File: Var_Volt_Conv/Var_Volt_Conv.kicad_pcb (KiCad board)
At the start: 6 copper layers, 101 x 65 mm, 100 parts, among them J101 Jack-DC, J102 Screw_Terminal_01x02, J103 Screw_Terminal_01x02, J201 Conn_01x05, Q101 AO3416, Q102 IRFML8244TRPBF, Q103 IRFML8244TRPBF, Q104 AO3407, Q105 AO3407, Q106 AO3407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

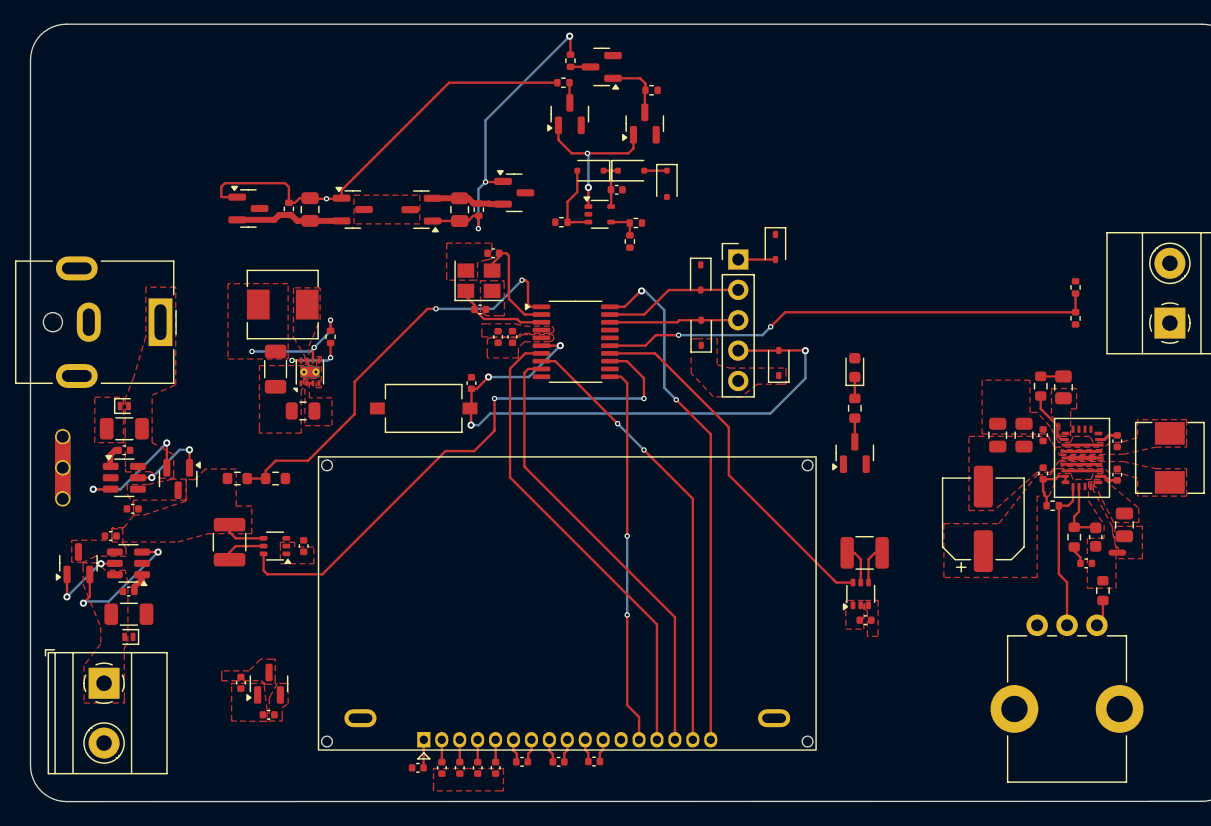
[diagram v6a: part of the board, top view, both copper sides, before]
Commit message: connected all traces, poured all copper pours, passed ERC
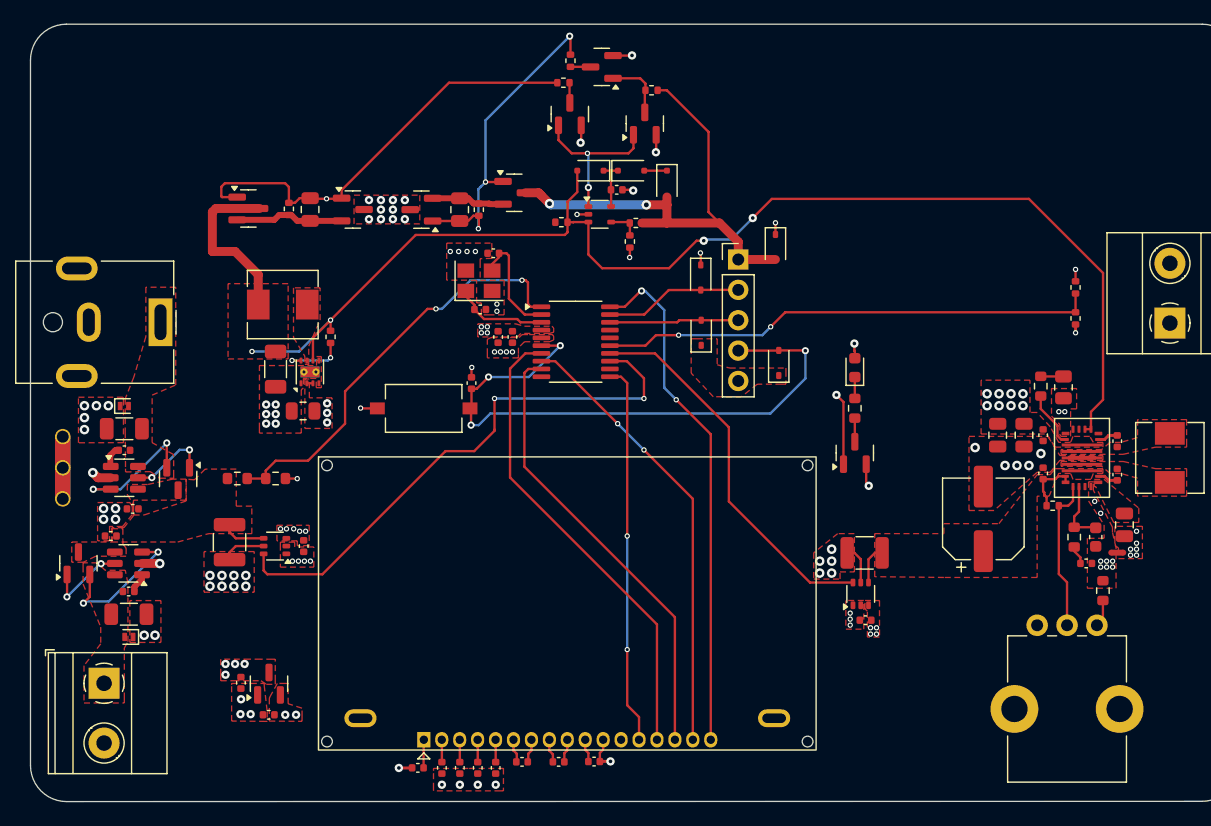
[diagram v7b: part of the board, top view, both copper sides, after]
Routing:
- net /[1] Power/BUCK_VOS: track 16.6 -> 122.4 mm, vias 3 -> 4
- net ST_3V3: track 3.11 -> 41.4 mm, vias 0 -> 2
- net GNDPWR: track 0.00 -> 14.3 mm, vias 0 -> 42
- net +3V3: track 0.00 -> 7.28 mm, vias 0 -> 29
- net GNDD: track 1.94 -> 8.18 mm, vias 0 -> 20
- net S-OUTPUT_CURRENT: track 30.8 -> 31.9 mm
- net VARIABLE_OUTPUT_VOLTAGE_B: track 3.31 -> 4.00 mm, vias 0 -> 6
- net SYSTEM_POWER_B: vias 0 -> 19
- net GNDA: vias 0 -> 17
- net +3V0: vias 0 -> 2
- added copper zone on In2.Cu, net +3V0
- added copper zone on In2.Cu, net +3V3
- added copper zone on In3.Cu, net GNDA
- added copper zone on In4.Cu, net GNDD
- added copper zone on In1.Cu, net GNDPWR
- added copper zone on In2.Cu, net SYSTEM_POWER_B
- added copper zone on F.Cu, net VARIABLE_OUTPUT_VOLTAGE_B
- added copper zone on In2.Cu, net VARIABLE_OUTPUT_VOLTAGE_B

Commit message: Updated power and analog ground connections of the buck converter
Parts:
- added NT103: NetTie_2, NetTie:NetTie-2_SMD_Pad0.5mm, F.Cu at (124.1, 96.6)
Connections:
- U104 pad 4: GNDPWR -> GNDA
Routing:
- net GNDA: track 0.00 -> 1.02 mm, vias 17 -> 18
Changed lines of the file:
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@@
 		(tags "capacitor")
 		(property "Reference" "C107"
-			(at 0 -1.16 360)
+			(at 0 -1.16 0)
 			(layer "F.SilkS")
 			(hide yes)
@@
 		)
 		(property "Value" "0.1uF"
-			(at 0 1.16 360)
+			(at 0 1.16 0)
 			(layer "F.Fab")
 			(effects
@@
 		)
 		(fp_text user "${REFERENCE}"
-			(at 0 0 360)
+			(at 0 0 0)
 			(layer "F.Fab")
 			(effects
@@
 		)
 	)
+	(footprint "NetTie:NetTie-2_SMD_Pad0.5mm"
+		(layer "F.Cu")
+		(at 124.1 96.6 -90)
+		(descr "Net tie, 2 pin, 0.5mm square SMD pads")
+		(tags "net tie")
+		(property "Reference" "NT103"
+			(at 0 -1.2 90)
+			(layer "F.SilkS")
+			(hide yes)
+			(effects
+				(font
+					(size 1 1)
+					(thickness 0.15)
+				)
+			)
+		)
+		(property "Value" "NetTie_2"
+			(at 0 1.2 90)
+			(layer "F.Fab")
+			(hide yes)
+			(effects
+				(font
+					(size 1 1)
+					(thickness 0.15)
+				)
+			)
+		)
+		(property "Footprint" "NetTie:NetTie-2_SMD_Pad0.5mm"
+			(at 0 0 -90)
+			(unlocked yes)
+			(layer "F.Fab")
+			(hide yes)
+			(effects
+				(font
+					(size 1.27 1.27)
+					(thickness 0.15)
+				)
+			)
+		)
+		(property "Datasheet" ""
+			(at 0 0 -90)
+			(unlocked yes)
+			(layer "F.Fab")
+			(hide yes)
+			(effects
+				(font
+					(size 1.27 1.27)
+					(thickness 0.15)
+				)
+			)
+		)
+		(property "Description" "Net tie, 2 pins"
+			(at 0 0 -90)
+			(unlocked yes)
+			(layer "F.Fab")
+			(hide yes)
+			(effects
+				(font
+					(size 1.27 1.27)
+					(thickness 0.15)
+				)
+			)
+		)
+		(property ki_fp_filters "Net*Tie*")
+		(sheetname "[1] Power")
+		(sheetfile "Power.kicad_sch")
+		(attr exclude_from_pos_files exclude_from_bom allow_missing_courtyard)
+		(net_tie_pad_groups "1, 2")
+		(fp_poly
+			(pts
+				(xy -0.5 -0.25) (xy 0.5 -0.25) (xy 0.5 0.25) (xy -0.5 0.25)
+			)
+			(stroke
+				(width 0)
+				(type solid)
+			)
+			(fill solid)
+			(layer "F.Cu")
+		)
+		(pad "1" smd circle
+			(at -0.5 0 270)
+			(size 0.5 0.5)
+			(layers "F.Cu")
+			(net 75 "GNDPWR")
+			(pinfunction "1")
+			(pintype "passive")
+		)
+		(pad "2" smd circle
+			(at 0.5 0 270)
+			(size 0.5 0.5)
+			(layers "F.Cu")
+			(net 76 "GNDA")
+			(pinfunction "2")
+			(pintype "passive")
+		)
+	)
 	(footprint "Capacitor_SMD:C_0805_2012Metric"
 		(layer "F.Cu")
@@
 			(layers "F.Cu" "F.Paste" "F.Mask")
 			(roundrect_rratio 0.25)
-			(net 75 "GNDPWR")
+			(net 76 "GNDA")
 			(pinfunction "AGND")
 			(pintype "power_in")
@@
 		(net 75)
 	)
+	(segment
+		(start 123.1125 97.125)
+		(end 124.025 97.125)
+		(width 0.2)
+		(layer "F.Cu")
+		(net 76)
+	)
+	(segment
+		(start 124.025 97.125)
+		(end 124.1 97.2)
+		(width 0.2)
+		(layer "F.Cu")
+		(net 76)
+	)
 	(via
 		(at 167.55 116.85)
@@
 	)
 	(via
+		(at 124.1 97.2)
+		(size 0.7)
+		(drill 0.3)
+		(layers "F.Cu" "B.Cu")
+		(free yes)
+		(net 76)
+	)
+	(via
 		(at 167.55 116.35)
 		(size 0.45)
@@
 		(polygon
 			(pts
-				(xy 118.1375 95.64) (xy 122.9125 95.64) (xy 122.9125 94.89) (xy 123.3125 94.89) (xy 123.3125 97.49)
-				(xy 122.8875 97.49) (xy 122.8875 96.715) (xy 121.8125 96.715) (xy 121.8125 97.515) (xy 121.6375 97.665)
+				(xy 118.1375 95.64) (xy 122.9125 95.64) (xy 122.9125 94.89) (xy 123.3125 94.89) (xy 123.3125 95.6)
+				(xy 124.4 95.6) (xy 124.4 96.6) (xy 122.8875 96.715) (xy 121.8125 96.715) (xy 121.8125 97.515) (xy 121.6375 97.665)
 				(xy 121.6375 101.29) (xy 118.1375 101.29) (xy 118.1375 100.915)
 			)
